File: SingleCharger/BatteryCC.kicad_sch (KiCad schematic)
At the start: 32 parts, among them Q1 TPHR8504PL,LQ(M1W, Q2 TPHR8504PL,LQ(M1W, Q3 L2N7002SLLT1G, U1 ADS1115IDGSR, U10 LM358, U11 MCP4725A0T-E/CH, U12 MCP4725A0T-E/CH, U8 UCC27324DR, U9 LM393

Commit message: wORKING ON REFACTOR
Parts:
- removed C20, C21: 100n, Resistor_SMD:R_1206_3216Metric_Pad1.30x1.75mm_HandSolder, symbol Device:C
- removed D3, D4: D, Diode_SMD:D_1206_3216Metric_Pad1.42x1.75mm_HandSolder, symbol Device:D
- removed Q1: TPHR8504PL,LQ(M1W, COMPONENTS:DFN-5_L4.9-W5.9-P1.27-LS6.2-BL, symbol COMPONENTS:TPHR8504PL,LQ(M1W
- removed Q3: L2N7002SLLT1G, COMPONENTS:SOT-23-3_L3.0-W1.7-P0.95-LS2.9-BR, symbol COMPONENTS:L2N7002SLLT1G
- removed R1: 0.003, Resistor_SMD:R_1206_3216Metric_Pad1.30x1.75mm_HandSolder, symbol Device:R
- removed R11: 100k, Resistor_SMD:R_1206_3216Metric_Pad1.30x1.75mm_HandSolder, symbol Device:R
- removed R13, R24, R25: 1k, Resistor_SMD:R_1206_3216Metric_Pad1.30x1.75mm_HandSolder, symbol Device:R
- removed R5, R9: 10k, Resistor_SMD:R_1206_3216Metric_Pad1.30x1.75mm_HandSolder, symbol Device:R
- removed U12: MCP4725A0T-E/CH, COMPONENTS:SOT-23-6_L2.9-W1.6-P0.95-LS2.8-BL, symbol COMPONENTS:MCP4725A0T-E_CH
- added C23, C24: 100n, Resistor_SMD:R_1206_3216Metric_Pad1.30x1.75mm_HandSolder, symbol Device:C
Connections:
- net 3v3GND is gone; now on net GND: C17.2, U1.1 (ADDR), U1.3 (GND)
- net +12V: now also C23.1, C24.1
- net B-: now also Q2.5 (D)
- net GND: now also C23.2, C24.2
- net Discharge: no longer names the net of U9.1
- net DischargeLV: no longer names the net of U8.2 (INA)
- net RSns Discharge: no longer names the net of U1.7 (AIN3)
- net RSns Discharge: no longer U9.2 (-)
- no-connect marks 2 -> 11
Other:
- moved on the sheet: U10B, U10C, U9A, U9C

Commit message: Rebuild
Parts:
- added R24, R25: 1k, Resistor_SMD:R_1206_3216Metric_Pad1.30x1.75mm_HandSolder, symbol Device:R
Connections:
- net +3V3: no longer C17.1, U1.8 (VDD)
- net RSns Charge: now also R24.2, R25.2; no longer R12.1, R22.2, U10.1
- net at R22.1, U9.6 (-): now also R24.1
- new net: R12.1, R22.2, R25.1, U10.1
- new net +5V: C17.1, U1.8 (VDD)
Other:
- moved on the sheet: C17

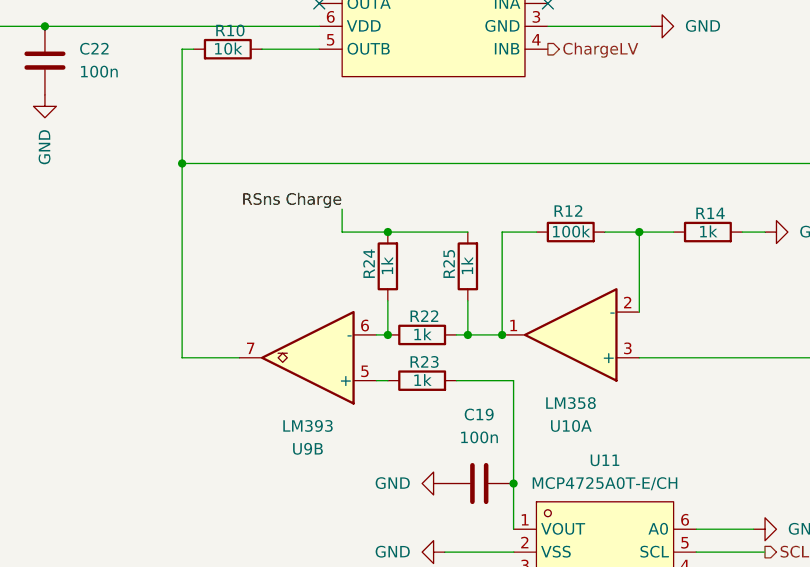
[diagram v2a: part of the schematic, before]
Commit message: Moved to +48V Feed. 25.2 Controlled by Pico.
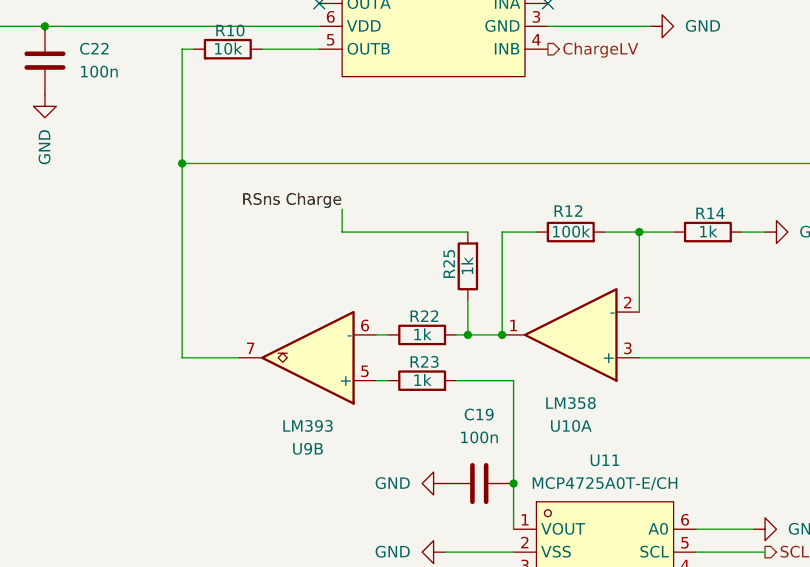
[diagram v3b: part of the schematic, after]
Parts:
- removed R24: 1k, Resistor_SMD:R_1206_3216Metric_Pad1.30x1.75mm_HandSolder, symbol Device:R
